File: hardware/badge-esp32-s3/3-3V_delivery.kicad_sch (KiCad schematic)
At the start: 13 parts, among them U2 NCP167BMX330TBG, U5 TPS63061DSCR

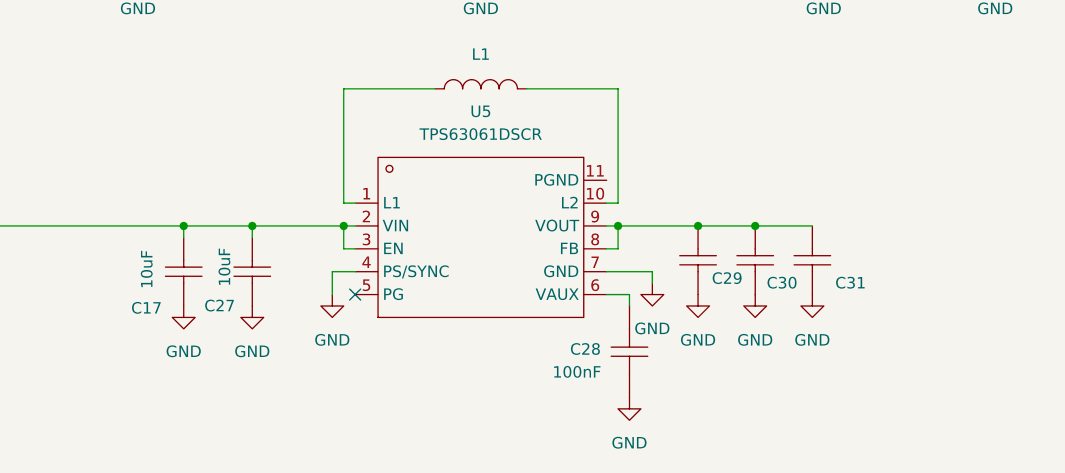
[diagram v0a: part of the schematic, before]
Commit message: Added the buck-boost converter. The traces aren't all connected though.
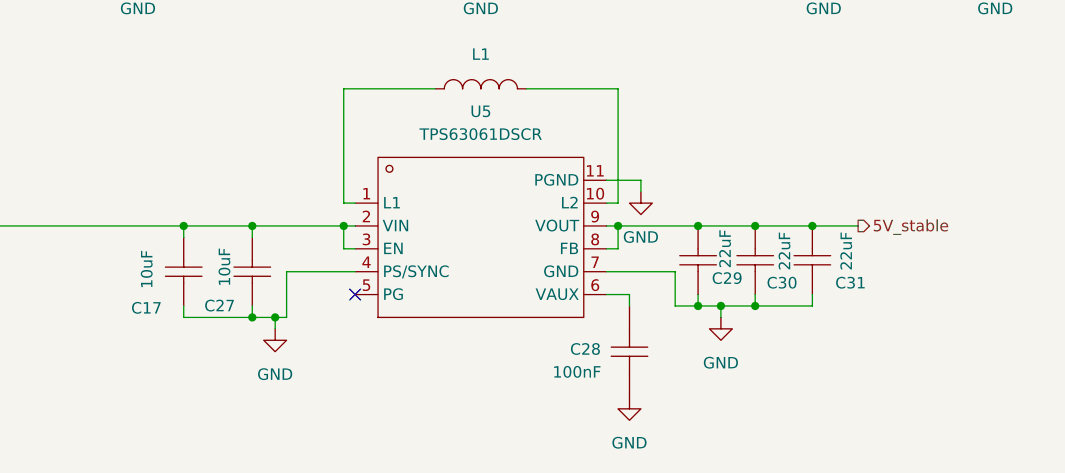
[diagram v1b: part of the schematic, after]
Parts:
- L1: footprint 1uH_inductor:IND-SMD_L4.0-W4.0_XFL4020-102MEB -> lcsc-lib:IND-SMD_L4.0-W4.0_XFL4020-102MEB
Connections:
- net GND: now also U5.11 (PGND)
- net 5V_stable: now reaches C29.2, C30.2, C31.2, U5.8 (FB), U5.9 (VOUT)

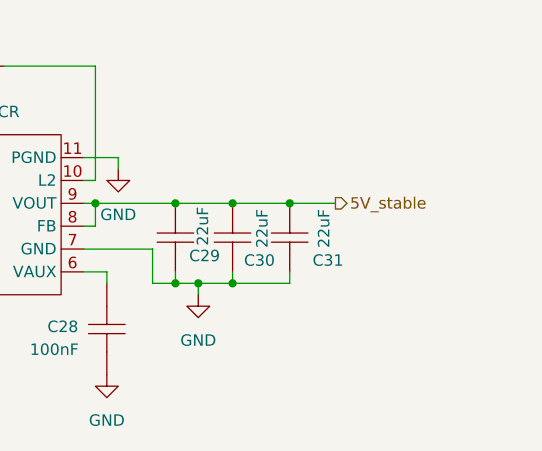
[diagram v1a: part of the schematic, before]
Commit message: Added thicker traces for the 5V circuit and added a TVS diode.
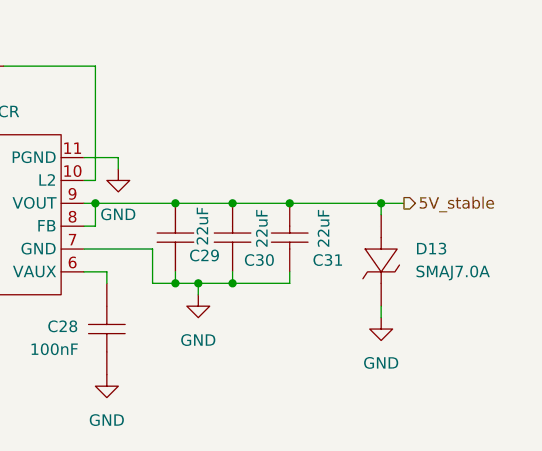
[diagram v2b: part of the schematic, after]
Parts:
- added D13: SMAJ7.0A, lcsc-lib:SMA_L4.5-W2.6-LS5.1-RD, symbol lcsc-lib:SMAJ7.0A_C2989694
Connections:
- net 5V_stable: now also D13.2 (A)
- net GND: now also D13.1 (K)
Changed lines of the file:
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@@
+	)
+	(junction
+		(at 193.04 110.49)
+		(diameter 0)
+		(color 0 0 0 0)
 	)
 	(junction
@@
 	(wire
 		(pts
+			(xy 193.04 123.19) (xy 193.04 121.92)
+		)
+		(stroke
+			(width 0)
+			(type default)
+		)
+	)
+	(wire
+		(pts
 			(xy 130.81 107.95) (xy 132.08 107.95)
 		)
@@
 	(wire
 		(pts
+			(xy 193.04 110.49) (xy 193.04 111.76)
+		)
+		(stroke
+			(width 0)
+			(type default)
+		)
+	)
+	(wire
+		(pts
 			(xy 120.65 120.65) (xy 120.65 119.38)
 		)
@@
 	(wire
 		(pts
-			(xy 182.88 110.49) (xy 187.96 110.49)
+			(xy 182.88 110.49) (xy 193.04 110.49)
 		)
 		(stroke
@@
 		(pts
 			(xy 170.18 119.38) (xy 167.64 119.38)
+		)
+		(stroke
+			(width 0)
+			(type default)
+		)
+	)
+	(wire
+		(pts
+			(xy 193.04 110.49) (xy 195.58 110.49)
 		)
 		(stroke
@@
 	(hierarchical_label "5V_stable"
 		(shape output)
-		(at 187.96 110.49 0)
+		(at 195.58 110.49 0)
 		(effects
 			(font
@@
 	)
 	(symbol
+		(lib_id "lcsc-lib:SMAJ7.0A_C2989694")
+		(at 193.04 116.84 90)
+		(unit 1)
+		(exclude_from_sim no)
+		(in_bom yes)
+		(on_board yes)
+		(dnp no)
+		(fields_autoplaced yes)
+		(property "Reference" "D13"
+			(at 196.85 115.5699 90)
+			(effects
+				(font
+					(size 1.27 1.27)
+				)
+				(justify right)
+			)
+		)
+		(property "Value" "SMAJ7.0A"
+			(at 196.85 118.1099 90)
+			(effects
+				(font
+					(size 1.27 1.27)
+				)
+				(justify right)
+			)
+		)
+		(property "Footprint" "lcsc-lib:SMA_L4.5-W2.6-LS5.1-RD"
+			(at 193.04 116.84 0)
+			(effects
+				(font
+					(size 1.27 1.27)
+				)
+				(hide yes)
+			)
+		)
+		(property "Datasheet" "https://item.szlcsc.com/datasheet/SMAJ7.0A/3449128.html"
+			(at 193.04 116.84 0)
+			(effects
+				(font
+					(size 1.27 1.27)
+				)
+				(hide yes)
+			)
+		)
+		(property "Description" "Polarity:Unidirectional Reverse Stand-Off Voltage (Vrwm):7V Clamping Voltage:12V Peak Pulse Current (Ipp):33.3A Peak Pulse Power Dissipation (Ppp):400W Voltage - Breakdown:7.78V Reverse Leakage Current (Ir):200uA Operating Temperature:-55°C~+150°C Operating"
+			(at 193.04 116.84 0)
+			(effects
+				(font
+					(size 1.27 1.27)
+				)
+				(hide yes)
+			)
+		)
+		(property "Manufacturer Part" "SMAJ7.0A"
+			(at 193.04 116.84 0)
+			(effects
+				(font
+					(size 1.27 1.27)
+				)
+				(hide yes)
+			)
+		)
+		(property "Manufacturer" "Liown(里阳半导体)"
+			(at 193.04 116.84 0)
+			(effects
+				(font
+					(size 1.27 1.27)
+				)
+				(hide yes)
+			)
+		)
+		(property "Supplier Part" "C2989694"
+			(at 193.04 116.84 0)
+			(effects
+				(font
+					(size 1.27 1.27)
+				)
+				(hide yes)
+			)
+		)
+		(property "Supplier" "LCSC"
+			(at 193.04 116.84 0)
+			(effects
+				(font
+					(size 1.27 1.27)
+				)
+				(hide yes)
+			)
+		)
+		(property "LCSC Part Name" "单向TVS 7V截止 峰值脉冲电流：33.3A"
+			(at 193.04 116.84 0)
+			(effects
+				(font
+					(size 1.27 1.27)
+				)
+				(hide yes)
+			)
+		)
+		(pin "2"
+		)
+		(pin "1"
+		)
+		(instances
+			(project ""
+				(path "/e2af9a6c-dbe9-4de2-9ba6-ea213a7300ec/f36e3e2c-eb39-474f-a489-171fecc16703"
+					(reference "D13")
+					(unit 1)
+				)
+			)
+		)
+	)
+	(symbol
 		(lib_id "lcsc-lib:TPS63061DSCR")
 		(at 146.05 111.76 0)
@@
 					(unit 1)
 				)
+			)
+		)
+	)
+	(symbol
+		(lib_id "power:GND")
+		(at 193.04 123.19 0)
+		(unit 1)
+		(exclude_from_sim no)
+		(in_bom yes)
+		(on_board yes)
+		(dnp no)
+		(fields_autoplaced yes)
+		(property "Reference" "#PWR050"
+			(at 193.04 129.54 0)
+			(effects
+				(font
+					(size 1.27 1.27)
+				)
+				(hide yes)
+			)
+		)
+		(property "Value" "GND"
+			(at 193.04 128.27 0)
+			(effects
+				(font
+					(size 1.27 1.27)
+				)
+			)
+		)
+		(property "Footprint" ""
+			(at 193.04 123.19 0)
+			(effects
+				(font
+					(size 1.27 1.27)
+				)
+				(hide yes)
+			)
+		)
+		(property "Datasheet" ""
+			(at 193.04 123.19 0)
+			(effects
+				(font
+					(size 1.27 1.27)
+				)
+				(hide yes)
+			)
+		)
+		(property "Description" "Power symbol creates a global label with name \"GND\" , ground"
+			(at 193.04 123.19 0)
+			(effects
+				(font
+					(size 1.27 1.27)
+				)
+				(hide yes)
+			)
+		)
+		(pin "1"
+		)
+		(instances
+			(project "badge-esp32-s3"
+				(path "/e2af9a6c-dbe9-4de2-9ba6-ea213a7300ec/f36e3e2c-eb39-474f-a489-171fecc16703"
+					(reference "#PWR050")
+					(unit 1)
+				)

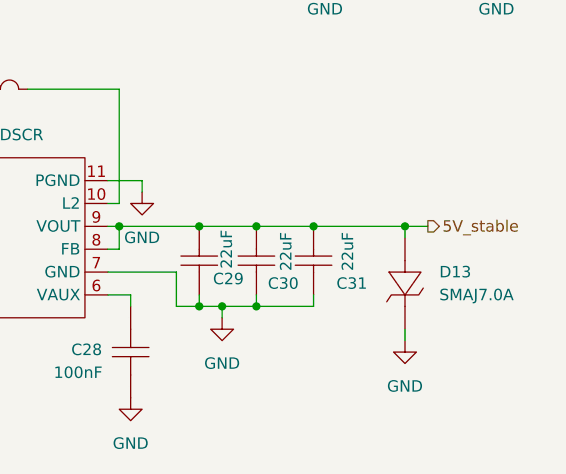
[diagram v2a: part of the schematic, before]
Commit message: Swapped the diode direction.
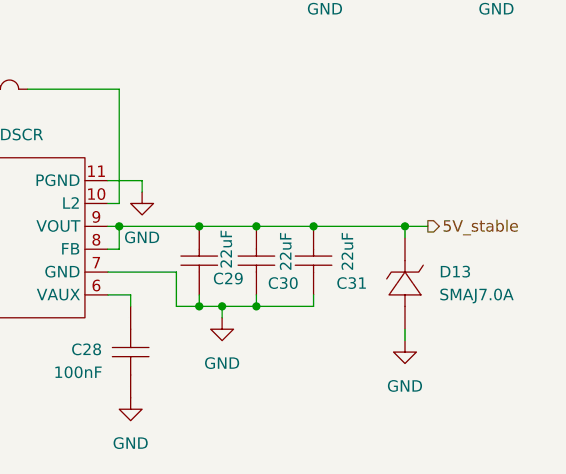
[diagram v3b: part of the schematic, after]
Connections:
- net 5V_stable: now also D13.1 (K); no longer D13.2 (A)
- net GND: now also D13.2 (A); no longer D13.1 (K)
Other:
- moved on the sheet: D13
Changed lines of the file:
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@@
 	(symbol
 		(lib_id "lcsc-lib:SMAJ7.0A_C2989694")
-		(at 193.04 116.84 90)
+		(at 193.04 116.84 270)
 		(unit 1)
 		(exclude_from_sim no)
@@
 					(size 1.27 1.27)
 				)
-				(justify right)
+				(justify left)
 			)
 		)
@@
 					(size 1.27 1.27)
 				)
-				(justify right)
+				(justify left)
 			)
 		)

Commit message: almost finished
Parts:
- removed U2: NCP167BMX330TBG, lcsc-lib:XDFN-4_L1.0-W1.0-P0.65-BL-EP, symbol lcsc-lib:NCP167BMX330TBG
- added C34: 100nF, PCM_JLCPCB:C_0402, symbol PCM_JLCPCB-Capacitors:0402,100nF
- added Q4: HL2301A, PCM_JLCPCB:Q_SOT-23, symbol PCM_JLCPCB-Transistors:PMOS,HL2301A
- added Q7: AO3424, lcsc-lib:SC-59-3_L2.9-W1.6-P0.95-LS2.9-BR, symbol lcsc-lib:AO3424
- added R41: 150kΩ, PCM_JLCPCB:R_0402, symbol PCM_JLCPCB-Resistors:0402,150kΩ
- added R44: 100kΩ, PCM_JLCPCB:R_0402, symbol PCM_JLCPCB-Resistors:0402,100kΩ
- added R46: 47kΩ, PCM_JLCPCB:R_0402, symbol PCM_JLCPCB-Resistors:0402,47kΩ
- added U8: TLV75733PDBVR, lcsc-lib:SOT-23-5_L2.9-W1.6-P0.95-LS2.8-BL, symbol lcsc-lib:TLV75733PDBVR
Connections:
- net GND: now also C34.2, Q7.2 (S), R46.2, U8.2 (GND)
- net VCC_3V3: now also Q7.1 (G), U8.5 (OUT)
- net VCC_5V: now also U8.1 (IN), U8.3 (EN)
- new net: Q4.3 (D), R41.1
- new net: Q4.1 (G), Q7.3 (D), R44.2
- new net VBATT: Q4.2 (S), R44.1
- new net V_Sense: C34.1, R41.2, R46.1
- no-connect marks 1 -> 2

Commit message: final changes and part updated
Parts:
- removed C28: 100nF, lcsc-lib:C0201, symbol lcsc-lib:CL03A104KP3NNNC
- added C24: 100nF, PCM_JLCPCB:C_0402, symbol PCM_JLCPCB-Capacitors:0402,100nF
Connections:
- net GND: now also C24.2
- net at U5.6 (VAUX): now also C24.1
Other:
- note added: "Resistor divider: Divides by 4.2 to bring the battery voltage down to about 1V... perfect for the esp32 0dB ADC attenuation mode."
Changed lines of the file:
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@@
 	(generator_version "9.0")
 	(paper "A4")
+	(text "Resistor divider:\n\nDivides by 4.2 to bring\nthe battery voltage down\nto about 1V... perfect\nfor the esp32 0dB ADC\nattenuation mode."
+		(exclude_from_sim no)
+		(at 25.654 164.084 0)
+		(effects
+			(font
+				(size 1.27 1.27)
+			)
+			(justify left)
+		)
+	)
 	(junction
 		(at 161.29 110.49)
@@
 	(wire
 		(pts
-			(xy 203.2 63.5) (xy 203.2 66.04)
+			(xy 162.56 118.11) (xy 162.56 120.65)
 		)
 		(stroke
@@
 	(wire
 		(pts
-			(xy 170.18 119.38) (xy 172.72 119.38)
+			(xy 203.2 63.5) (xy 203.2 66.04)
 		)
 		(stroke
@@
 	(wire
 		(pts
-			(xy 69.85 173.99) (xy 69.85 177.8)
+			(xy 170.18 119.38) (xy 172.72 119.38)
 		)
 		(stroke
@@
 	(wire
 		(pts
-			(xy 38.1 123.19) (xy 38.1 125.73)
+			(xy 69.85 173.99) (xy 69.85 177.8)
 		)
 		(stroke
@@
 	(wire
 		(pts
-			(xy 59.69 134.62) (xy 71.12 134.62)
+			(xy 38.1 123.19) (xy 38.1 125.73)
 		)
 		(stroke
@@
 	(wire
 		(pts
-			(xy 130.81 113.03) (xy 132.08 113.03)
+			(xy 59.69 134.62) (xy 71.12 134.62)
 		)
 		(stroke
@@
 	(wire
 		(pts
-			(xy 162.56 118.11) (xy 162.56 119.38)
+			(xy 130.81 113.03) (xy 132.08 113.03)
 		)
 		(stroke
@@
 	(wire
 		(pts
+			(xy 162.56 128.27) (xy 162.56 129.54)
+		)
+		(stroke
+			(width 0)
+			(type default)
+		)
+	)
+	(wire
+		(pts
 			(xy 107.95 63.5) (xy 107.95 68.58)
 		)
@@
 	)
 	(symbol
-		(lib_id "power:GND")
-		(at 184.15 81.28 0)
+		(lib_id "PCM_JLCPCB-Capacitors:0402,100nF")
+		(at 162.56 124.46 0)
 		(unit 1)
 		(exclude_from_sim no)
@@
 		(on_board yes)
 		(dnp no)
-		(fields_autoplaced yes)
-		(property "Reference" "#PWR06"
-			(at 184.15 87.63 0)
+		(property "Reference" "C24"
+			(at 165.1 121.9199 0)
 			(effects
 				(font
 					(size 1.27 1.27)
 				)
-				(hide yes)
+				(justify left)
 			)
 		)
-		(property "Value" "GND"
-			(at 184.15 86.36 0)
+		(property "Value" "100nF"
+			(at 165.1 124.46 0)
+			(effects
+				(font
+					(size 0.8 0.8)
+				)
+				(justify left)
+			)
+		)
+		(property "Footprint" "PCM_JLCPCB:C_0402"
+			(at 160.782 124.46 90)
 			(effects
 				(font
 					(size 1.27 1.27)
 				)
+				(hide yes)
 			)
 		)
-		(property "Footprint" ""
-			(at 184.15 81.28 0)
+		(property "Datasheet" "https://www.lcsc.com/datasheet/lcsc_datasheet_2304140030_Samsung-Electro-Mechanics-CL05B104KO5NNNC_C1525.pdf"
+			(at 162.56 124.46 0)
 			(effects
 				(font
@@
 			)
 		)
-		(property "Datasheet" ""
-			(at 184.15 81.28 0)
+		(property "Description" "16V 100nF X7R ±10% 0402 Multilayer Ceramic Capacitors MLCC - SMD/SMT ROHS"
+			(at 162.56 124.46 0)
 			(effects
 				(font
@@
 			)
 		)
-		(property "Description" "Power symbol creates a global label with name \"GND\" , ground"
-			(at 184.15 81.28 0)
+		(property "LCSC" "C1525"
+			(at 162.56 124.46 0)
 			(effects
 				(font
@@
 			)
 		)
-		(pin "1"
+		(property "Stock" "20208285"
+			(at 162.56 124.46 0)
+			(effects
+				(font
+					(size 1.27 1.27)
+				)
+				(hide yes)
+			)
 		)
-		(instances
-			(project ""
-				(path "/e2af9a6c-dbe9-4de2-9ba6-ea213a7300ec/f36e3e2c-eb39-474f-a489-171fecc16703"
-					(reference "#PWR06")
-					(unit 1)
+		(property "Price" "0.004USD"
+			(at 162.56 124.46 0)
+			(effects
+				(font
+					(size 1.27 1.27)
 				)
+				(hide yes)
 			)
 		)
-	)
-	(symbol
-		(lib_id "lcsc-lib:CL03A104KP3NNNC")
-		(at 162.56 124.46 90)
-		(unit 1)
-		(exclude_from_sim no)
-		(in_bom yes)
-		(on_board yes)
-		(dnp no)
-		(property "Reference" "C28"
-			(at 155.956 124.206 90)
+		(property "Process" "SMT"
+			(at 162.56 124.46 0)
 			(effects
 				(font
 					(size 1.27 1.27)
 				)
-				(justify right)
+				(hide yes)
 			)
 		)
-		(property "Value" "100nF"
-			(at 156.718 126.746 90)
+		(property "Minimum Qty" "20"
+			(at 162.56 124.46 0)
 			(effects
 				(font
 					(size 1.27 1.27)
 				)
+				(hide yes)
 			)
 		)
-		(property "Footprint" "lcsc-lib:C0201"
+		(property "Attrition Qty" "10"
 			(at 162.56 124.46 0)
 			(effects
@@
 			)
 		)
-		(property "Datasheet" "https://item.szlcsc.com/datasheet/CL03A104KP3NNNC/50070.html"
+		(property "Class" "Basic Component"
 			(at 162.56 124.46 0)
 			(effects
@@
 			)
 		)
-		(property "Description" "Capacitance:100nF Tolerance:±10% Tolerance:±10% Voltage Rating:10V Temperature Coefficient:X5R"
+		(property "Category" "Capacitors,Multilayer Ceramic Capacitors MLCC - SMD/SMT"
 			(at 162.56 124.46 0)
 			(effects
@@
 			)
 		)
-		(property "Manufacturer Part" "CL03A104KP3NNNC"
+		(property "Manufacturer" "Samsung Electro-Mechanics"
 			(at 162.56 124.46 0)
 			(effects
@@
 			)
 		)
-		(property "Manufacturer" "SAMSUNG(三星)"
+		(property "Part" "CL05B104KO5NNNC"
 			(at 162.56 124.46 0)
 			(effects
@@
 			)
 		)
-		(property "Supplier Part" "C49062"
+		(property "Voltage Rated" "16V"
+			(at 165.1 127 0)
+			(effects
+				(font
+					(size 0.8 0.8)
+				)
+				(justify left)
+			)
+		)
+		(property "Tolerance" "±10%"
 			(at 162.56 124.46 0)
 			(effects
@@
 			)
 		)
-		(property "Supplier" "LCSC"
+		(property "Capacitance" "100nF"
 			(at 162.56 124.46 0)
 			(effects
@@
 			)
 		)
-		(property "LCSC Part Name" "100nF ±10% 10V"
+		(property "Temperature Coefficient" "X7R"
 			(at 162.56 124.46 0)
 			(effects
@@
 			)
 		)
+		(pin "2"
+		)
 		(pin "1"
 		)
-		(pin "2"
+		(instances
+			(project ""
+				(path "/e2af9a6c-dbe9-4de2-9ba6-ea213a7300ec/f36e3e2c-eb39-474f-a489-171fecc16703"
+					(reference "C24")
+					(unit 1)
+				)
+			)
+		)
+	)
+	(symbol
+		(lib_id "power:GND")
+		(at 184.15 81.28 0)
+		(unit 1)
+		(exclude_from_sim no)
+		(in_bom yes)
+		(on_board yes)
+		(dnp no)
+		(fields_autoplaced yes)
+		(property "Reference" "#PWR06"
+			(at 184.15 87.63 0)
+			(effects
+				(font
+					(size 1.27 1.27)
+				)
+				(hide yes)
+			)
+		)
+		(property "Value" "GND"
+			(at 184.15 86.36 0)
+			(effects
+				(font
+					(size 1.27 1.27)
+				)
+			)
+		)
+		(property "Footprint" ""
+			(at 184.15 81.28 0)
+			(effects
+				(font
+					(size 1.27 1.27)
+				)
+				(hide yes)
+			)
+		)
+		(property "Datasheet" ""
+			(at 184.15 81.28 0)
+			(effects
+				(font
+					(size 1.27 1.27)
+				)
+				(hide yes)
+			)
+		)
+		(property "Description" "Power symbol creates a global label with name \"GND\" , ground"
+			(at 184.15 81.28 0)
+			(effects
+				(font
+					(size 1.27 1.27)
+				)
+				(hide yes)
+			)
+		)
+		(pin "1"
 		)
 		(instances
 			(project ""
 				(path "/e2af9a6c-dbe9-4de2-9ba6-ea213a7300ec/f36e3e2c-eb39-474f-a489-171fecc16703"
-					(reference "C28")
+					(reference "#PWR06")
 					(unit 1)
 				)

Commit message: finished component alignment
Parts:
- L1: LCSC (none) -> C5355380; Supplier Part C5355380 -> (none)
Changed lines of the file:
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@@
 			)
 		)
-		(property "Supplier Part" "C5355380"
+		(property "LCSC" "C5355380"
 			(at 146.05 95.25 0)
 			(effects
